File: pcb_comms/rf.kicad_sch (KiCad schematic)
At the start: 25 parts, among them J4 Conn_Coaxial, U2 CG2179M2

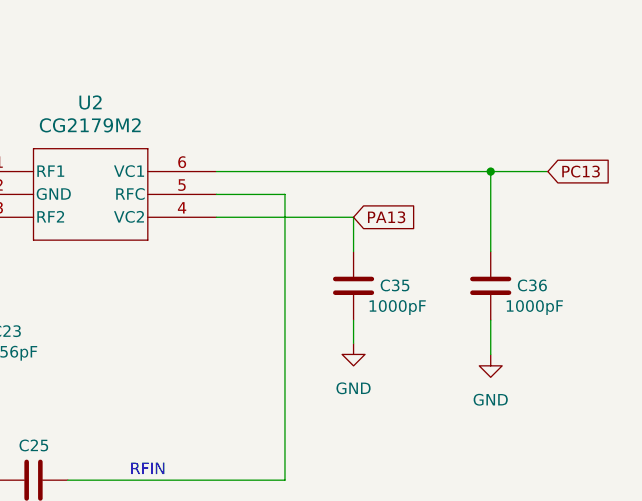
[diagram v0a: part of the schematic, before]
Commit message: Add usb and gps
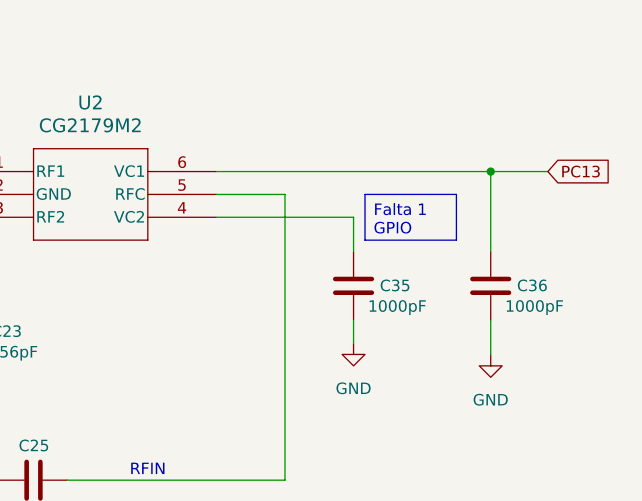
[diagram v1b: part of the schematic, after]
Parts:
- U2: footprint MINISO6_CG21_CEL -> (none)
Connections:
- net PA13: no longer names the net of C35.2, U2.4 (VC2)
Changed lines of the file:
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@@
+		)
+	)
+	(text_box "Falta 1 GPIO\n"
+		(exclude_from_sim no)
+		(at 224.79 76.2 0)
+		(size 10.16 5.08)
+		(margins 0.9525 0.9525 0.9525 0.9525)
+		(stroke
+			(width 0)
+			(type solid)
+		)
+		(fill
+			(type none)
+		)
+		(effects
+			(font
+				(size 1.27 1.27)
+			)
+			(justify left top)
 		)
 	)
@@
 		)
 	)
-	(global_label "PA13"
-		(shape input)
-		(at 223.52 78.74 0)
-		(fields_autoplaced yes)
-		(effects
-			(font
-				(size 1.27 1.27)
-			)
-			(justify left)
-		)
-		(property "Intersheetrefs" "${INTERSHEET_REFS}"
-			(at 231.2828 78.74 0)
-			(effects
-				(font
-					(size 1.27 1.27)
-				)
-				(justify left)
-				(hide yes)
-			)
-		)
-	)
 	(global_label "RFO_HP"
 		(shape input)
@@
 			)
 		)
-		(property "Footprint" "MINISO6_CG21_CEL"
+		(property "Footprint" ""
 			(at 194.564 85.09 0)
 			(effects
@@
 			)
 		)
-		(property "Datasheet" "CG2179M2"
+		(property "Datasheet" ""
 			(at 194.056 83.312 0)
 			(effects

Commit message: Update GPS
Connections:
- net RF_CRL2_TO_STM32: now reaches C35.2, U2.4 (VC2)
- net PC13 renamed RF_CRL1_TO_STM32
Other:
- moved on the sheet: C13, C15, C17, C18, C19, C20, C21, C22, C23, C24, C25, C27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

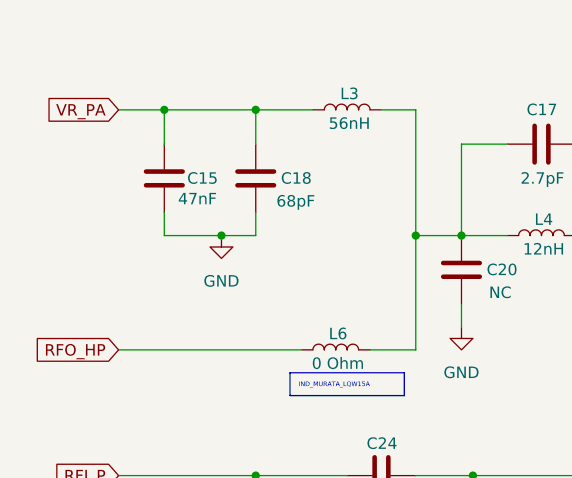
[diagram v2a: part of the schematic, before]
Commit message: Add antenna deploy
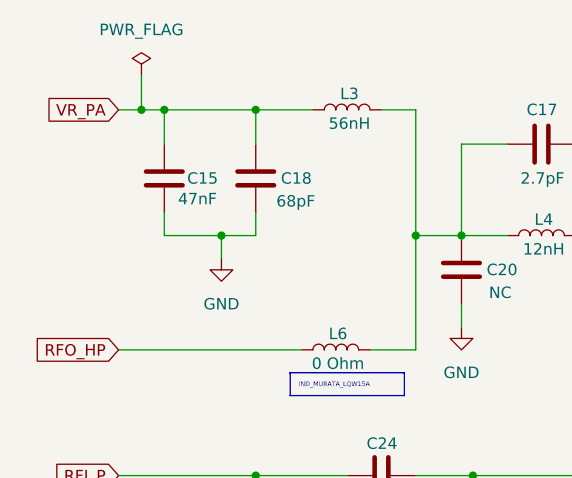
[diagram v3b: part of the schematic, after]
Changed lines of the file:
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@@
+	)
+	(junction
+		(at 52.07 44.45)
+		(diameter 0)
+		(color 0 0 0 0)
 	)
 	(junction
@@
 	(wire
 		(pts
+			(xy 52.07 44.45) (xy 54.61 44.45)
+		)
+		(stroke
+			(width 0)
+			(type default)
+		)
+	)
+	(wire
+		(pts
 			(xy 64.77 95.25) (xy 49.53 95.25)
 		)
@@
 	(wire
 		(pts
-			(xy 49.53 44.45) (xy 54.61 44.45)
+			(xy 49.53 44.45) (xy 52.07 44.45)
 		)
 		(stroke
@@
 	(wire
 		(pts
+			(xy 52.07 40.64) (xy 52.07 44.45)
+		)
+		(stroke
+			(width 0)
+			(type default)
+		)
+	)
+	(wire
+		(pts
 			(xy 88.9 96.52) (xy 88.9 85.09)
 		)
@@
 		(pts
 			(xy 64.77 85.09) (xy 64.77 86.36)
+		)
+		(stroke
+			(width 0)
+			(type default)
+		)
+	)
+	(wire
+		(pts
+			(xy 60.96 60.96) (xy 60.96 58.42)
 		)
 		(stroke
@@
 	)
 	(symbol
+		(lib_id "power:PWR_FLAG")
+		(at 52.07 40.64 0)
+		(unit 1)
+		(exclude_from_sim no)
+		(in_bom yes)
+		(on_board yes)
+		(dnp no)
+		(fields_autoplaced yes)
+		(property "Reference" "#FLG04"
+			(at 52.07 38.735 0)
+			(effects
+				(font
+					(size 1.27 1.27)
+				)
+				(hide yes)
+			)
+		)
+		(property "Value" "PWR_FLAG"
+			(at 52.07 35.56 0)
+			(effects
+				(font
+					(size 1.27 1.27)
+				)
+			)
+		)
+		(property "Footprint" ""
+			(at 52.07 40.64 0)
+			(effects
+				(font
+					(size 1.27 1.27)
+				)
+				(hide yes)
+			)
+		)
+		(property "Datasheet" "~"
+			(at 52.07 40.64 0)
+			(effects
+				(font
+					(size 1.27 1.27)
+				)
+				(hide yes)
+			)
+		)
+		(property "Description" "Special symbol for telling ERC where power comes from"
+			(at 52.07 40.64 0)
+			(effects
+				(font
+					(size 1.27 1.27)
+				)
+				(hide yes)
+			)
+		)
+		(pin "1"
+		)
+		(instances
+			(project ""
+				(path "/ea597178-b44d-4db9-826c-8f86e8d231f0/f2ec5e10-3e2b-4fad-b66b-c622a3150eea"
+					(reference "#FLG04")
+					(unit 1)
+				)
+			)
+		)
+	)
+	(symbol
 		(lib_id "power:GND")
 		(at 107.95 68.58 0)
@@
 	)
 	(symbol
-		(lib_name "CG2179M2_1")
 		(lib_id "MINISO6_CG21_CEL:CG2179M2")
 		(at 180.34 60.96 0)
@@
 			)
 		)
-		(property "Datasheet" ""
+		(property "Datasheet" "CG2179M2"
 			(at 180.086 68.072 0)
 			(effects
@@
 	(symbol
 		(lib_id "power:GND")
-		(at 60.96 58.42 0)
+		(at 60.96 60.96 0)
 		(unit 1)
 		(exclude_from_sim no)
@@
 		(fields_autoplaced yes)
 		(property "Reference" "#PWR017"
-			(at 60.96 64.77 0)
+			(at 60.96 67.31 0)
 			(effects
 				(font
@@
 		)
 		(property "Value" "GND"
-			(at 60.96 63.5 0)
-			(effects
-				(font
-					(size 1.27 1.27)
-				)
-			)
-		)
-		(property "Footprint" ""
-			(at 60.96 58.42 0)
+			(at 60.96 66.04 0)
+			(effects
+				(font
+					(size 1.27 1.27)
+				)
+			)
+		)
+		(property "Footprint" ""
+			(at 60.96 60.96 0)
 			(effects
 				(font
@@
 		)
 		(property "Datasheet" ""
-			(at 60.96 58.42 0)
+			(at 60.96 60.96 0)
 			(effects
 				(font
@@
 		)
 		(property "Description" "Power symbol creates a global label with name \"GND\" , ground"
-			(at 60.96 58.42 0)
-			(effects
-				(font
+			(at 60.96 60.96 0)
+			(effects
+				(font

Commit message: Last update
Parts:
- removed C20: NC, symbol Device:C
- removed C27: NC (0402), symbol Device:C
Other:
- company: (none) -> Sanie Peralta, Alejandro Campo
- title: (none) -> PC1: APRS & GPS
- moved on the sheet: C17

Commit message: rev 1.1
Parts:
- removed J4: Conn_Coaxial, symbol Connector:Conn_Coaxial
- added AE1: Antenna_Shield, symbol Device:Antenna_Shield
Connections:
- net GND: now also AE1.2 (Shield)
- net at C28.2, L7.1: now also AE1.1 (A)
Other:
- note added: "50 Ohms"
- moved on the sheet: C19, C25, C28, C29, L7

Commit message: Finish schematic
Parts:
- removed C36: 1000pF, symbol Device:C
- removed U2: CG2179M2, symbol MINISO6_CG21_CEL:CG2179M2
- added C27: 10pF, symbol Device:C
- added IC4: BGS12WN6E6329XTSA1, symbol RF_SWITCH_BGS12WN6E6329XTSA1:BGS12WN6E6329XTSA1
- added R19, R20: 100R, symbol Device:R
- C13: value 56pF -> 68pF
- C23: value 56pF -> 10pF
- C25: value 56pF -> 1nF
- C35: value 1000pF -> 1nF
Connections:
- net RF_CRL2_TO_STM32 is gone; now on net GND: C35.2
- net GND: now also C23.2, C25.2, C27.2, IC4.2 (GND); no longer C35.1
- net at C22.1, L5.2: now also IC4.1 (RF2); no longer C13.1
- net at C13.2: now also IC4.5 (RFIN)
- net at C24.2: now also IC4.3 (RF1); no longer C23.1
- net at C29.2, L7.2: now also C13.1; no longer C25.1
- new net: C23.1, C25.1, IC4.4 (VDD), R19.1
- new net: C27.1, C35.1, IC4.6 (CTRL), R20.1
- new net RF_CRL_TO_STM32: R20.2
- new net VDDRF: R19.2
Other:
- moved on the sheet: AE1, C21, C28, C29, L7

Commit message: Version 1.0. No DRA yet
From now on I will make the connections for IIS and then adapt it for the club
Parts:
- L6: value 0 Ohm -> 0R
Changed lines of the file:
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@@
 		)
 	)
-	(text_box "IND_MURATA_LQW15A"
+	(text_box "RCS04020000Z0ED"
 		(exclude_from_sim no)
-		(at 68.58 73.66 0)
-		(size 12.7 2.54)
+		(at 69.215 73.66 0)
+		(size 9.525 2.54)
 		(margins 0.9525 0.9525 0.9525 0.9525)
 		(stroke
@@
 			)
 		)
-		(property "Value" "0 Ohm"
+		(property "Value" "0R"
 			(at 73.914 72.644 90)
 			(effects

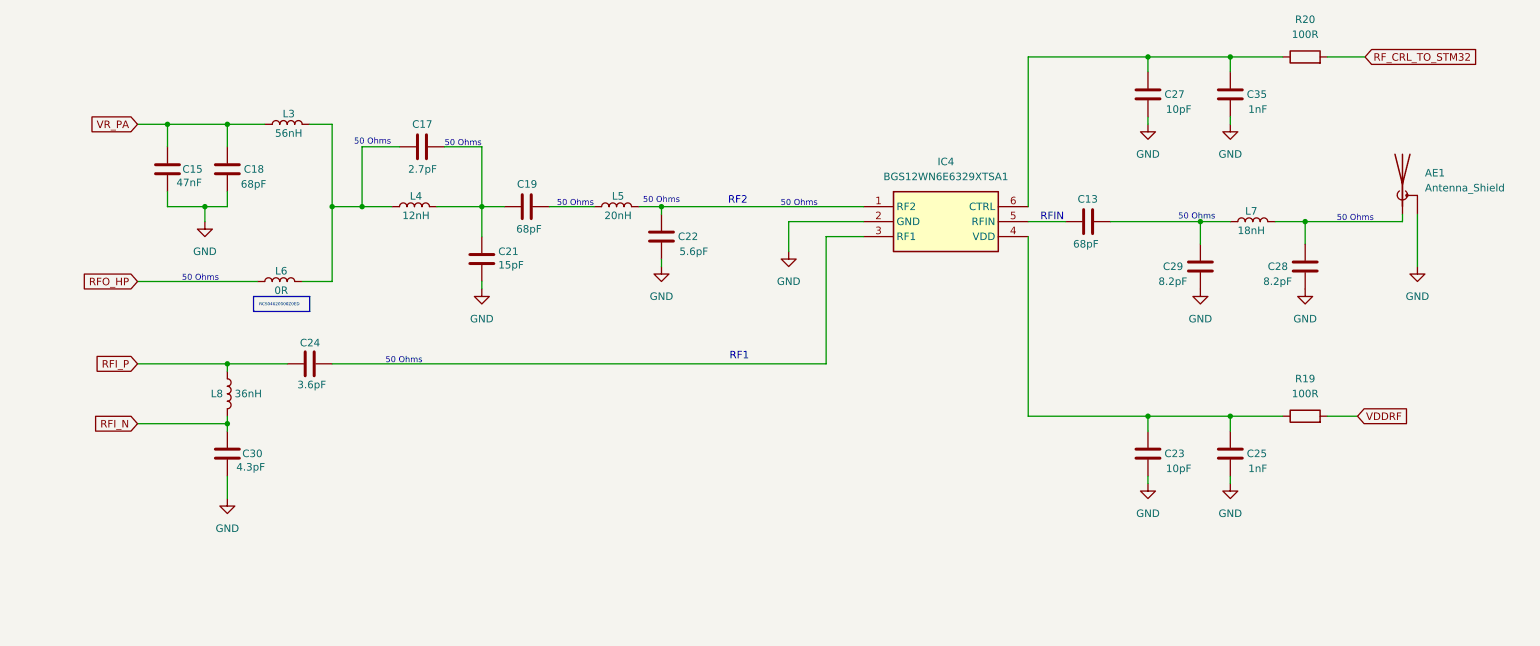
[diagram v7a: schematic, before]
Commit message: Add footprints
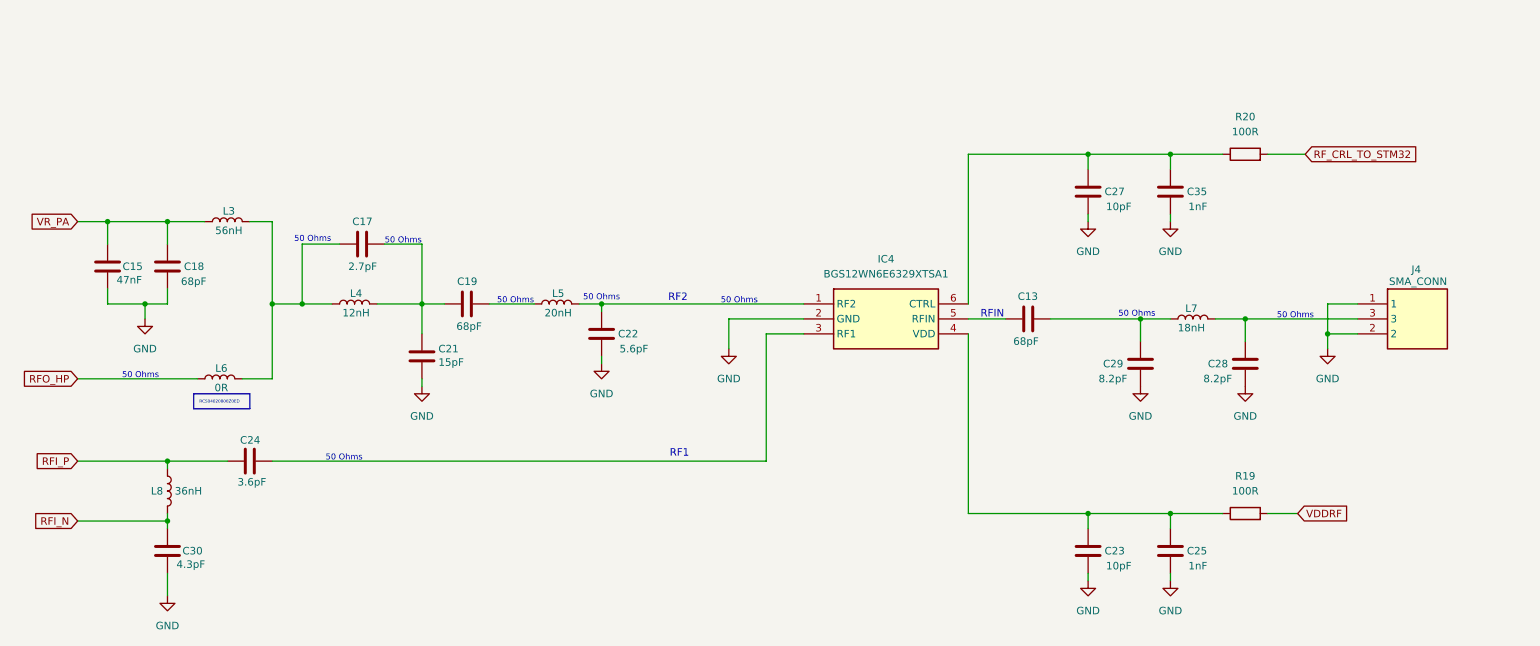
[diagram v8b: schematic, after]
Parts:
- removed AE1: Antenna_Shield, symbol Device:Antenna_Shield
- added J4: SMA_CONN, SMA_ANTENNA_CONSMA002-SMD-G:SMA_ANTENNA_CONSMA002-SMD-G, symbol SMA_ANTENNA_CONSMA002-SMD-G:CONSMA002-SMD-G
- C13, C15, C17, C18, C19, C21, C22, C23, C24, C25, C27, C28, C29, C30, C35: footprint (none) -> Capacitor_SMD:C_0805_2012Metric_Pad1.18x1.45mm_HandSolder
- IC4: footprint (none) -> RF_SWITCH_BGS12WN6E6329XTSA1:BGS12WN6E6329XTSA1
- L3, L7: footprint (none) -> Inductor_SMD:L_0805_2012Metric_Pad1.05x1.20mm_HandSolder
- L4, L8: footprint (none) -> Inductor_0805_2015metric:Inductor_0805_2015metric
- L5, L6: footprint (none) -> Inductor_SMD:L_0402_1005Metric_Pad0.77x0.64mm_HandSolder
- R19, R20: footprint (none) -> Resistor_SMD:R_0805_2012Metric_Pad1.20x1.40mm_HandSolder
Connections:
- net GND: now also J4.1, J4.2
- net at C28.2, L7.1: now also J4.3
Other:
- moved on the sheet: C13, C15, C17, C18, C19, C21, C22, C23, C24, C25, C27, C28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
